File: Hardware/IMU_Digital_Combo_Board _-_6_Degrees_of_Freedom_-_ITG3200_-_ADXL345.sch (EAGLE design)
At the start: 17 parts, among them U1 ADXL345, U3 ITG-32001:1

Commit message: Proper CC 3.0 Attribution
Added proper CC 3.0 attribution in board and schematic.
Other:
- note added: "Revised by: Kade Jensen"
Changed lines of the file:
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@@
 <text x="68.58" y="99.06" size="1.778" layer="97">0xD0 for write, 0xD1 for read</text>
 <text x="63.5" y="15.24" size="1.778" layer="97">0xA6 for write, 0xA7 for read</text>
+<text x="175.26" y="25.4" size="1.778" layer="96">Revised by: Kade Jensen</text>
 </plain>
 <instances>

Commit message: Updated ADXL345 Package and connected SDA signal
SDA trace had gotten dropped in previous design by accident. Reconnected
now and took the opportunity to include new ADXL345 footprint. Had to
change the route job significantly to make it all fit.
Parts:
- U1: value ADXL345 -> ADXL3451:1; device SparkFun:ADXL345 -> Testing:ADXL3451:1
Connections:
- net 3.3V: now also U3.VDD
- net SDA: now also U3.SDA
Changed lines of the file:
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@@
 <parts>
 <part name="FRAME1" library="SparkFun" deviceset="FRAME-LETTER" device=""/>
-<part name="U1" library="SparkFun" deviceset="ADXL345" device=""/>
+<part name="U1" library="Testing" deviceset="ADXL345" device="1:1"/>
 <part name="C1" library="SparkFun" deviceset="CAP" device="0603-CAP" value="0.1uF"/>
 <part name="C2" library="SparkFun" deviceset="CAP" device="0603-CAP" value="0.1uF"/>
@@
 </segment>
 <segment>
-<wire x1="66.04" y1="144.78" x2="63.5" y2="144.78" width="0.1524" layer="91"/>
 <wire x1="63.5" y1="144.78" x2="63.5" y2="147.32" width="0.1524" layer="91"/>
 <pinref part="P+5" gate="G$1" pin="3.3V"/>
+<pinref part="U3" gate="G$1" pin="VDD"/>
+<wire x1="63.5" y1="144.78" x2="66.04" y2="144.78" width="0.1524" layer="91"/>
 </segment>
 <segment>
@@
 <pinref part="JP1" gate="G$1" pin="3"/>
 <label x="187.96" y="111.76" size="1.27" layer="95" rot="R180" xref="yes"/>
-</segment>
-</net>
+<pinref part="U3" gate="G$1" pin="SDA"/>
+</segment>
+</net>

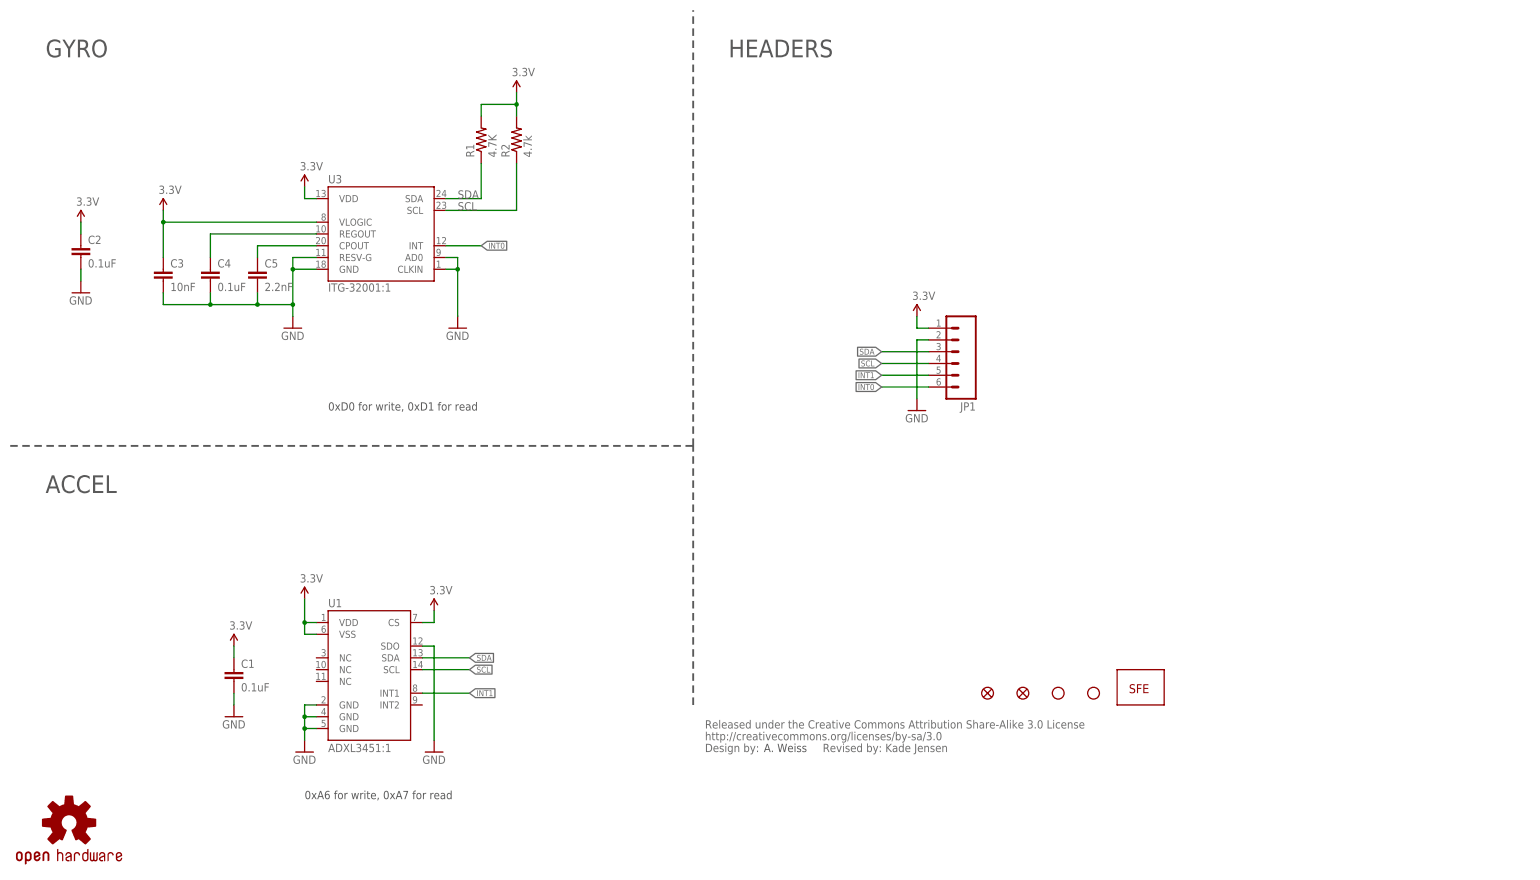
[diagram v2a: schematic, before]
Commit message: Updating README,  cleaning up board files, adding library
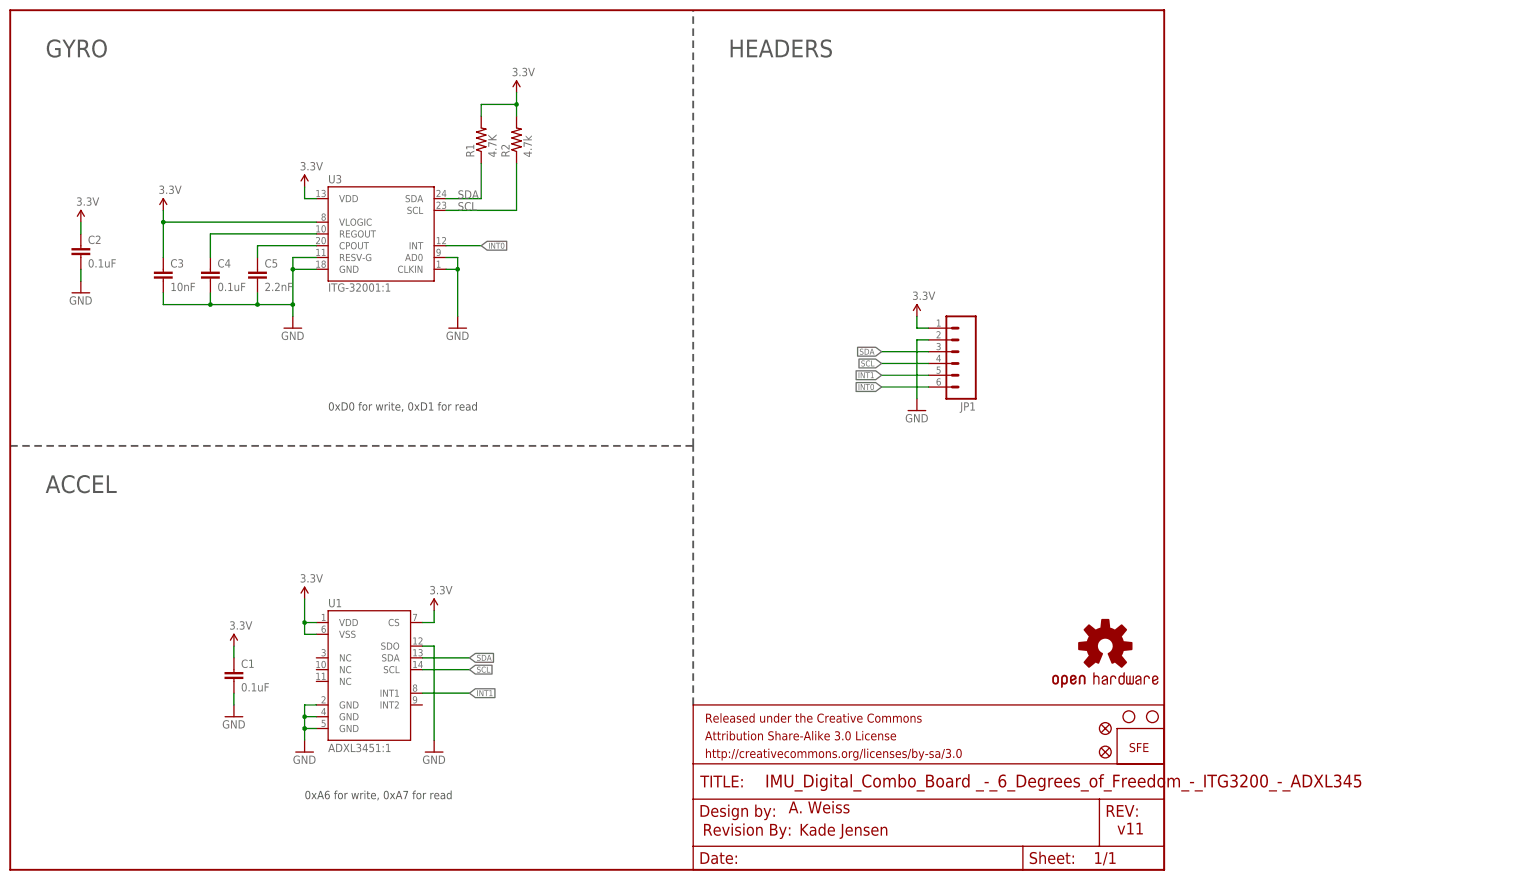
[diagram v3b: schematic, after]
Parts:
- added FRAME1: FRAME-LETTER, SparkFun-Aesthetics:FRAME-LETTER
- U$1: value CREATIVE_COMMONS -> REVISION; device SparkFun:CREATIVE_COMMONS -> SparkFun-Aesthetics:REVISION
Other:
- note added: "Kade Jensen"
- note added: "v11"
- note removed: "Revised by: Kade Jensen"
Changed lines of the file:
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@@
 <?xml version="1.0" encoding="utf-8"?>
 <!DOCTYPE eagle SYSTEM "eagle.dtd">
-<eagle version="6.4">
+<eagle version="6.5.0">
 <drawing>
 <settings>
@@
 </classes>
 <parts>
-<part name="FRAME1" library="SparkFun" deviceset="FRAME-LETTER" device=""/>
+<part name="FRAME1" library="SparkFun-Aesthetics" deviceset="FRAME-LETTER" device=""/>
 <part name="U1" library="Testing" deviceset="ADXL345" device="1:1"/>
 <part name="C1" library="SparkFun" deviceset="CAP" device="0603-CAP" value="0.1uF"/>
@@
 <part name="C5" library="SparkFun" deviceset="CAP" device="0603-CAP" value="2.2nF"/>
 <part name="GND3" library="SparkFun" deviceset="GND" device=""/>
-<part name="U$1" library="SparkFun" deviceset="CREATIVE_COMMONS" device=""/>
 <part name="P+7" library="SparkFun" deviceset="3.3V" device=""/>
 <part name="GND8" library="SparkFun" deviceset="GND" device=""/>
@@
 <part name="JP4" library="SparkFun" deviceset="FIDUCIAL" device="1X2"/>
 <part name="JP6" library="SparkFun" deviceset="FIDUCIAL" device="1X2"/>
+<part name="U$1" library="SparkFun-Aesthetics" deviceset="REVISION" device=""/>
 </parts>
 <sheets>
@@
 <wire x1="147.32" y1="35.56" x2="147.32" y2="91.44" width="0.4064" layer="97" style="shortdash"/>
 <wire x1="147.32" y1="91.44" x2="147.32" y2="185.42" width="0.4064" layer="97" style="shortdash"/>
-<text x="162.56" y="25.4" size="1.778" layer="97">A. Weiss</text>
+<text x="167.894" y="12.192" size="2.54" layer="94">A. Weiss</text>
 <text x="7.62" y="175.26" size="3.81" layer="97">GYRO</text>
 <text x="7.62" y="81.28" size="3.81" layer="97">ACCEL</text>
@@
 <text x="68.58" y="99.06" size="1.778" layer="97">0xD0 for write, 0xD1 for read</text>
 <text x="63.5" y="15.24" size="1.778" layer="97">0xA6 for write, 0xA7 for read</text>
-<text x="175.26" y="25.4" size="1.778" layer="96">Revised by: Kade Jensen</text>
+<text x="170.18" y="7.366" size="2.54" layer="94">Kade Jensen</text>
+<text x="238.76" y="7.62" size="2.54" layer="94">v11</text>
 </plain>
 <instances>
@@
 <instance part="C5" gate="G$1" x="53.34" y="127"/>
 <instance part="GND3" gate="1" x="60.96" y="116.84"/>
-<instance part="U$1" gate="G$1" x="149.86" y="25.4"/>
 <instance part="P+7" gate="G$1" x="195.58" y="119.38"/>
 <instance part="GND8" gate="1" x="195.58" y="99.06"/>
-<instance part="JP3" gate="G$1" x="241.3" y="38.1"/>
+<instance part="JP3" gate="G$1" x="241.3" y="25.4"/>
 <instance part="P+6" gate="G$1" x="33.02" y="142.24"/>
 <instance part="GND1" gate="1" x="96.52" y="116.84"/>
@@
 <instance part="GND6" gate="1" x="91.44" y="25.4"/>
 <instance part="JP1" gate="G$1" x="203.2" y="111.76" rot="R180"/>
-<instance part="JP2" gate="G$1" x="233.68" y="38.1"/>
-<instance part="JP5" gate="G$1" x="226.06" y="38.1"/>
-<instance part="U$2" gate="G$1" x="12.7" y="10.16"/>
+<instance part="JP2" gate="G$1" x="246.38" y="33.02"/>
+<instance part="JP5" gate="G$1" x="241.3" y="33.02"/>
+<instance part="U$2" gate="G$1" x="236.22" y="48.26"/>
 <instance part="U3" gate="G$1" x="78.74" y="137.16"/>
-<instance part="JP4" gate="G$1" x="218.44" y="38.1"/>
-<instance part="JP6" gate="G$1" x="210.82" y="38.1"/>
+<instance part="JP4" gate="G$1" x="236.22" y="25.4"/>
+<instance part="JP6" gate="G$1" x="236.22" y="30.48"/>
+<instance part="U$1" gate="G$1" x="149.352" y="7.366"/>
 </instances>
 <busses>
